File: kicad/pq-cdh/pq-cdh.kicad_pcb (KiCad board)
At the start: 4 copper layers, 43 x 43 mm, 35 parts, among them IC1 STM32L496RGT3, IC2 IS25LP128F-JBLA3, J1 Conn_01x04, J2 Conn_01x16, J3 Conn_01x04, J4 Conn_01x04, J5 Conn_01x16, J6 Conn_01x04, J7 Conn_02x06_Odd_Even, J8 Conn_01x04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

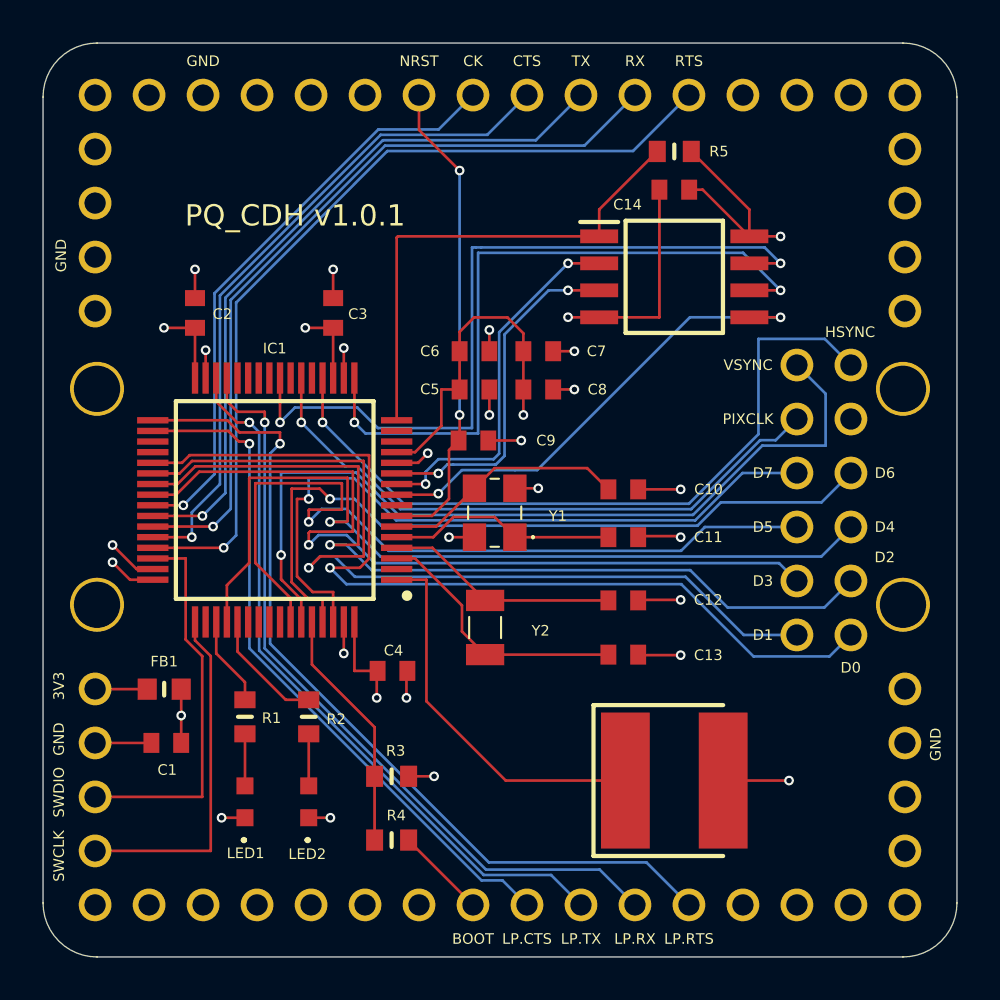
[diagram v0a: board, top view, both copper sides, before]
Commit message: With Changes related Ext Flash SPI configuration
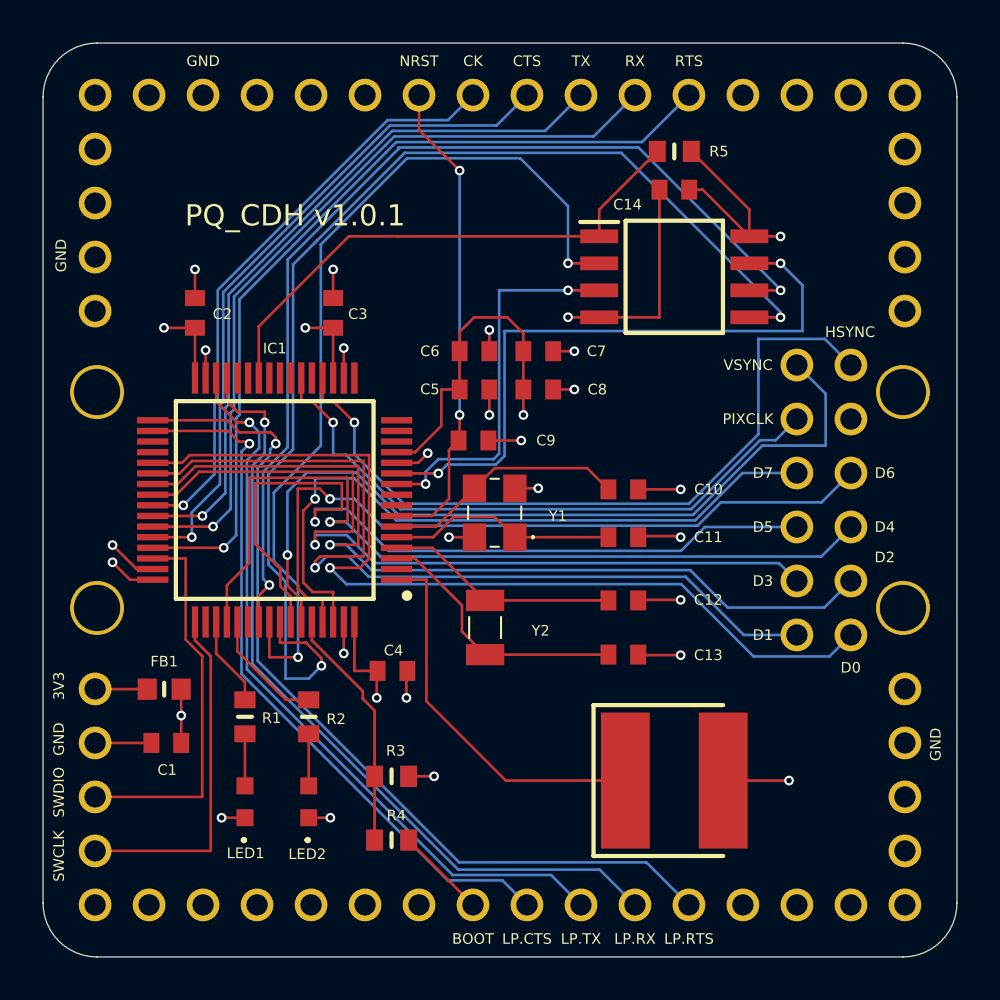
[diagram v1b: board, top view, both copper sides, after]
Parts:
- moved J6 0.15 mm to (155.0, 108.0)
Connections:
- IC1 pad 10: /QUADSPI_BK2_IO1 -> /IO1_WP
- IC1 pad 11: /QUADSPI_BK2_IO2 -> /IO2_HR
- IC1 pad 16: /QUADSPI_BK1_NCS -> unconnected-(IC1-Pad16)
- IC1 pad 17: /QUADSPI_CLK -> unconnected-(IC1-Pad17)
- IC1 pad 24: /QUADSPI_BK2_IO3 -> unconnected-(IC1-Pad24)
- IC1 pad 26: unconnected-(IC1-Pad26) -> /SPI1_NSS
- IC1 pad 55: unconnected-(IC1-Pad55) -> /SPI1_SCK
- IC1 pad 56: unconnected-(IC1-Pad56) -> /SPI1_MISO
- IC1 pad 57: unconnected-(IC1-Pad57) -> /SPI1_MOSI
- IC1 pad 9: /QUADSPI_BK2_IO0 -> unconnected-(IC1-Pad9)
- IC2 pad 1: /QUADSPI_BK1_NCS -> /SPI1_NSS
- IC2 pad 2: /QUADSPI_BK2_IO1 -> /SPI1_MISO
- IC2 pad 3: /QUADSPI_BK2_IO2 -> /IO1_WP
- IC2 pad 5: /QUADSPI_BK2_IO0 -> /SPI1_MOSI
- IC2 pad 6: /QUADSPI_CLK -> /SPI1_SCK
- IC2 pad 7: /QUADSPI_BK2_IO3 -> /IO2_HR
- R5 pad 2: /QUADSPI_BK1_NCS -> /SPI1_NSS
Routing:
- net /SPI1_MOSI: track 0.00 -> 55.7 mm, vias 0 -> 2
- net /SPI1_SCK: track 0.00 -> 47.5 mm, vias 0 -> 2
- net /SPI1_MISO: track 0.00 -> 42.2 mm, vias 0 -> 2
- net /QUADSPI_BK2_IO3: track 36.6 -> 0.00 mm, vias 2 -> 0
- net /QUADSPI_CLK: track 33.1 -> 0.00 mm, vias 2 -> 0
- net /IO2_HR: track 0.00 -> 30.4 mm, vias 0 -> 2
- net /SPI1_NSS: track 0.00 -> 25.3 mm
- net /QUADSPI_BK1_NCS: track 23.3 -> 0.00 mm
- net /QUADSPI_BK2_IO0: track 23.0 -> 0.00 mm, vias 2 -> 0
- net /IO1_WP: track 0.00 -> 18.1 mm, vias 0 -> 2
- net /QUADSPI_BK2_IO1: track 17.5 -> 0.00 mm, vias 2 -> 0
- net /QUADSPI_BK2_IO2: track 16.5 -> 0.00 mm, vias 2 -> 0
- net /LPUART_TX: track 34.1 -> 35.4 mm
- net /LPUART_RX: track 36.6 -> 37.9 mm
- net /LPUART_CTS: track 32.5 -> 33.7 mm
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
